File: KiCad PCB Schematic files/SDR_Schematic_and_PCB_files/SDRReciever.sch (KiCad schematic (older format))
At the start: 80 parts, among them J1 Conn_Coaxial, J10 I_0, J11 I_180, J12 Q_90, J13 Q_270, J14 I_OUT, J15 Q_OUT, J16 5V, J17 4.3V, J18 Conn_01x02_Female, J19 Conn_01x02_Female, J2 AudioJack3, J3 FIL_I, J4 FIL_O, J5 CLK_1, J6 CLK_2, J7 CLK_0, J8 I_LO, J9 Q_LO, Q1 PN2222A, U1 Si5351A-B-GT, U2 74AC74, U3 SN74CBT3253, U4 INA821ID, U5 INA821ID, U6 OP213FPZ, U7 LM741, Y1 ATS250

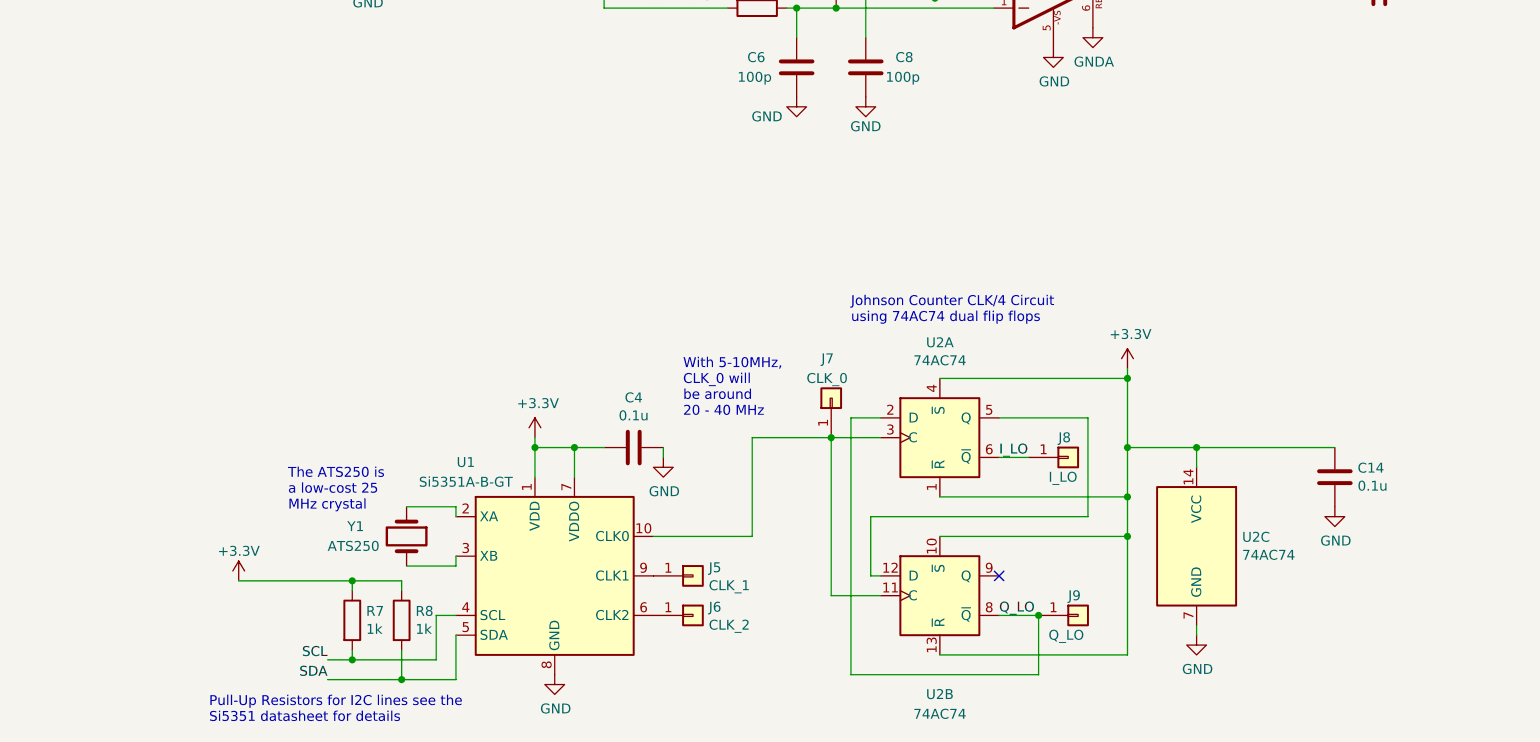
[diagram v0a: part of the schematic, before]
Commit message: Removed unnecessary files and components
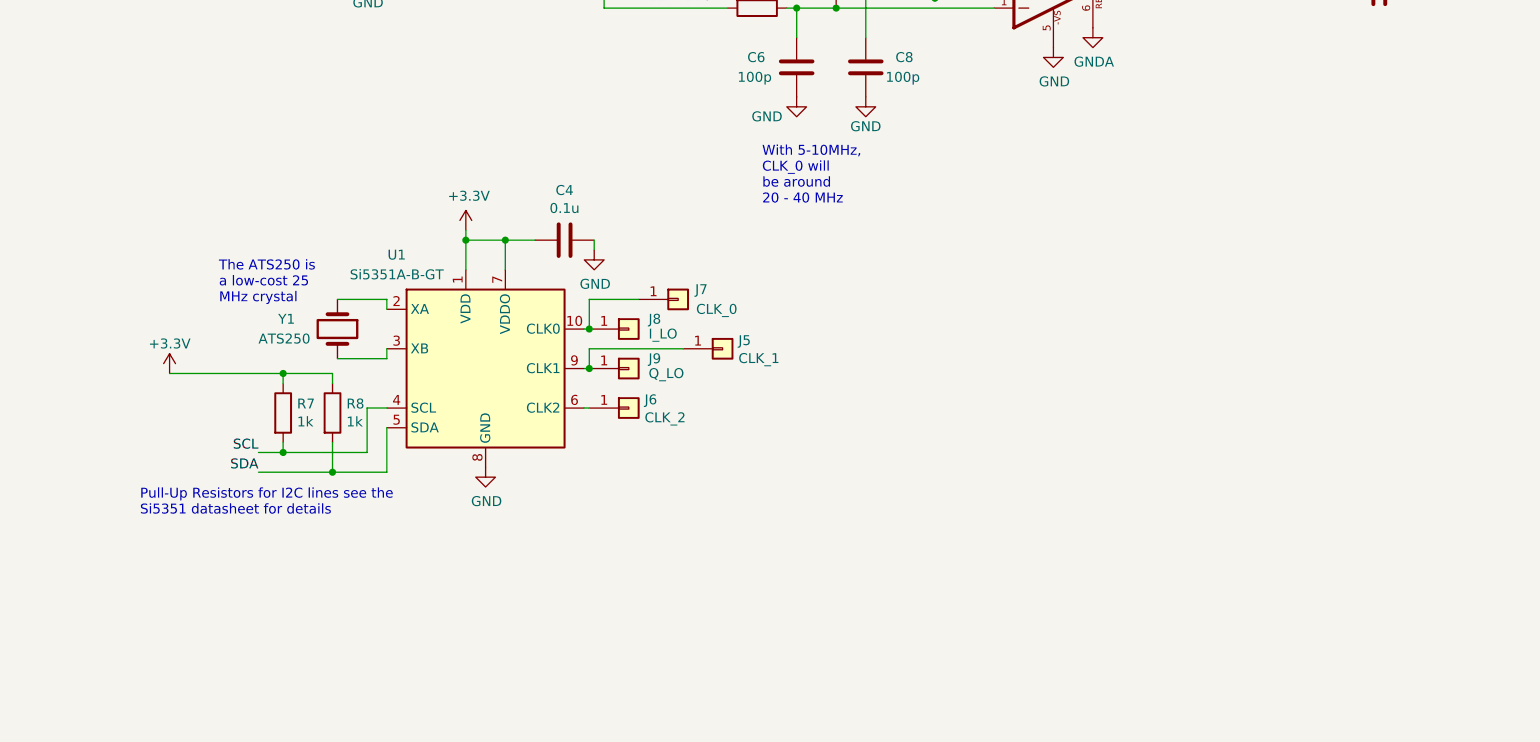
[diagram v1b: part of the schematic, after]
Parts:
- removed C14: 0.1u, Capacitor_THT:C_Disc_D5.1mm_W3.2mm_P5.00mm, symbol SDRReciever-rescue:C-Device
- removed U2: 74AC74, Package_DIP:DIP-14_W7.62mm, symbol SDRReciever-rescue:74HC74-74xx
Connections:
- net I_LO: no longer J8.1 (Pin_1)
- net Q_LO: no longer J9.1 (Pin_1)
- net at J7.1 (Pin_1), U1.10 (CLK0): now also J8.1 (Pin_1)
- net at J5.1 (Pin_1), U1.9 (CLK1): now also J9.1 (Pin_1)
- no-connect marks 27 -> 26
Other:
- note removed: "Johnson Counter CLK/4 Circuit\nusing 74AC74 dual flip flops"
- moved on the sheet: C4, J5, J6, J7, J8, J9, R7, R8, U1, Y1

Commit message: Updated values for bandpass filter in KiCad schematic Now a 3-rd order, series first, butterworth filter passing 6-16Mhz Also added some additional comments to KiCad schematic
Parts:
- removed RV1: 100k, symbol SDRReciever-rescue:R_POT-Device
- added R18, R19: 10k, Resistor_THT:R_Axial_DIN0207_L6.3mm_D2.5mm_P7.62mm_Horizontal, symbol SDRReciever-rescue:R-Device
- C2: value 910pF -> 330pF
- C3: value 150pF -> 330pF
- L1: value 820nH -> 430nH
- L2: value 560nH -> 820nH
- L3: value 3.6uH -> 820nH
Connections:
- net +4.3V: now also R18.2
- net BPF_OUT: now also R18.1, R19.2
- net GND: now also R19.1
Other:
- note added: "2.15V Voltage Bias to center\nthe incoming frequency between \nmax and min input values for tayloe mixer"
- note added: "6-16MHz (3rd Order, Series-First Butterworth)\nBy doing Series-First, DC signals cannot pass through the capacitor (C2), \nallowing better control over the DC offset going into the op-amps"
- note added: "Amplifiers"
- note added: "Antenna Connector"
- note added: "Arduino Nano"
- note added: "Bandpass Filter"
- note added: "C5-C8 are sampling\ncapacitors which also\nact as low pass filters here"
- note added: "Final Output\n(to soundcard)"
- note added: "Local Oscillator (Si5351a)"
- note added: "Low Pass Filter (2-Pole)"
- note added: "NOTE:\nDouble check values of C5-C8"
- note added: "T37-6 Toroid:\n-- turns"
- note added: "T50-6 Toroid: \n-- turns"
- note added: "Tayloe Mixer"
- note added: "Test point pad"
- note added: "To smooth 5V power supply from\nUSB which may contain noise"
- note added: "Voltage Smoother"
- note removed: "Bandpass Filter 5-18MHz (3rd Order, Series-First Bessel)\nBy doing Series-First, DC signals cannot pass through the capacitor (C2), \nallowing better control over the DC offset going into the op-amps"
- note removed: "T37-6 Toroid:\n17 turns"
- note removed: "T50-6 Toroid: \n12 turns"
- note removed: "T50-6 Toroid: \n30 turns"
- note removed: "Tunable\n2.15V Bias"
- note removed: "With 5-10MHz, \nCLK_0 will \nbe around \n20 - 40 MHz"
- moved on the sheet: A1, C11, C12, C13, C4, J5, J6, J7, J8, J9, JP2, R7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

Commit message: Updated schematic, added voltage converter and comments
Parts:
- removed J8: I_LO, Connector_PinHeader_2.54mm:PinHeader_1x01_P2.54mm_Vertical, symbol SDRReciever-rescue:Conn_01x01-Connector_Generic
- removed J9: Q_LO, Connector_PinHeader_2.54mm:PinHeader_1x01_P2.54mm_Vertical, symbol SDRReciever-rescue:Conn_01x01-Connector_Generic
- added Q2, Q3: BSS138, Package_TO_SOT_SMD:SOT-23, symbol Device:Q_NMOS_GSD
- added R20, R21, R22, R23: 10k, Resistor_SMD:R_0805_2012Metric, symbol SDRReciever-rescue:R-Device
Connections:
- net +3V3: now also Q2.1 (G), Q3.1 (G), R20.1, R21.1
- net +4.3V: now also U7.7 (V+)
- net +5V: now also R22.1, R23.1; no longer U7.7 (V+)
- net I_LO: now also J7.1 (Pin_1), U1.10 (CLK0)
- net Q_LO: now also J5.1 (Pin_1), U1.9 (CLK1)
- net SCL renamed SCL_3V
- net SCL_3V: now also Q3.2 (S), R21.2; no longer A1.24 (A5)
- net SDA renamed SDA_3V
- net SDA_3V: now also Q2.2 (S), R20.2; no longer A1.23 (A4)
- new net SCL_5V: A1.24 (A5), Q3.3 (D), R23.2
- new net SDA_5V: A1.23 (A4), Q2.3 (D), R22.2
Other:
- note added: "5V to 3.3V Conveter"
- note added: "NOTE: maybe split the gain between these two op amp stages (especially if the later stage is low noise)"
- note added: "NOTE: use Lower noise op amp"
- note added: "NOTE:\nDouble check values of C5-C8\n100nf?"
- note added: "Note:\nCheck all footprints\nExchange some through hole components for surface mount"
- note added: "This is used to convert the\n5V logic of the arduino nano\nto the 3.3V logic of the Si5351a\nboth directions."
- note removed: "NOTE:\nDouble check values of C5-C8"
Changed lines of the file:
@@
 EESchema Schematic File Version 4
-LIBS:SDRReciever-cache
-EELAYER 26 0
+EELAYER 30 0
 EELAYER END
 $Descr A1 33110 23386
@@
 $EndComp
 Text Label 14250 4725 1    50   ~ 0
-SDA
+SDA_5V
 Text Label 14350 4725 1    50   ~ 0
-SCL
+SCL_5V
 $Comp
 L SDRReciever-rescue:+3.3V-power #PWR02
@@
 $EndComp
 Text Label 7475 5850 2    50   ~ 0
-SDA
+SDA_3V
 Text Label 7475 5750 2    50   ~ 0
-SCL
+SCL_3V
 $Comp
 L SDRReciever-rescue:Jumper_NC_Small-Device JP2
@@
 $EndComp
 $Comp
-L SDRReciever-rescue:Conn_01x01-Connector_Generic J8
-U 1 1 5EAFA8DE
-P 9350 5125
-F 0 "J8" H 9450 5175 50  0000 L CNN
-F 1 "I_LO" H 9450 5100 50  0000 L CNN
-F 2 "Connector_PinHeader_2.54mm:PinHeader_1x01_P2.54mm_Vertical" H 9350 5125 50  0001 C CNN
-F 3 "~" H 9350 5125 50  0001 C CNN
-	1    9350 5125
-	1    0    0    -1
-$EndComp
-$Comp
-L SDRReciever-rescue:Conn_01x01-Connector_Generic J9
-U 1 1 5EB14DFD
-P 9350 5325
-F 0 "J9" H 9450 5375 50  0000 L CNN
-F 1 "Q_LO" H 9450 5300 50  0000 L CNN
-F 2 "Connector_PinHeader_2.54mm:PinHeader_1x01_P2.54mm_Vertical" H 9350 5325 50  0001 C CNN
-F 3 "~" H 9350 5325 50  0001 C CNN
-	1    9350 5325
-	1    0    0    -1
-$EndComp
-$Comp
 L SDRReciever-rescue:C-Device C17
 U 1 1 5EA7D591
@@
 	1    0    0    -1
 $EndComp
-$Comp
-L SDRReciever-rescue:+5V-power #PWR042
-U 1 1 5EDC9E45
-P 4625 4325
-F 0 "#PWR042" H 4625 4175 50  0001 C CNN
-F 1 "+5V" H 4775 4375 50  0000 C CNN
-F 2 "" H 4625 4325 50  0001 C CNN
-F 3 "" H 4625 4325 50  0001 C CNN
-	1    4625 4325
-	1    0    0    -1
-$EndComp
 Wire Wire Line
 	4425 4725 4325 4725
@@
 	5025 4625 5425 4625
 Connection ~ 5025 4625
-Text Notes 4125 4150 0    50   ~ 0
+Text Notes 4175 4075 0    50   ~ 0
 The INA821ID Amps require the REF\ninput to have a voltage source with a\nlow output impedence. The LM741\nvoltage buffer handles this
 Wire Wire Line
@@
 Wire Notes Line
 	5000 1600 5000 1650
-Text Notes 6875 6075 0    50   ~ 0
+Text Notes 6875 6175 0    50   ~ 0
 Pull-Up Resistors for I2C lines see the \nSi5351 datasheet for details
 Wire Wire Line
@@
 Wire Wire Line
 	9150 5325 9125 5325
-Connection ~ 9150 5325
 Wire Wire Line
 	9150 5125 9125 5125
-Connection ~ 9150 5125
 Wire Wire Line
 	9150 5525 9125 5525
@@
 Amplifiers
 Text Notes 6400 2775 0    50   ~ 0
-NOTE:\nDouble check values of C5-C8
+NOTE:\nDouble check values of C5-C8\n100nf?
+Text Notes 4600 5600 0    50   ~ 0
+NOTE: use Lower noise op amp
+Text Notes 13250 3800 0    50   ~ 0
+NOTE: maybe split the gain between these two op amp stages (especially if the later stage is low noise)
+$Comp
+L SDRReciever-rescue:R-Device R20
+U 1 1 607EFC63
+P 2400 7025
+F 0 "R20" H 2470 7071 50  0000 L CNN
+F 1 "10k" H 2470 6980 50  0000 L CNN
+F 2 "Resistor_SMD:R_0805_2012Metric" V 2330 7025 50  0001 C CNN
+F 3 "~" H 2400 7025 50  0001 C CNN
+	1    2400 7025
+	1    0    0    -1
+$EndComp
+Wire Wire Line
+	4050 6825 4050 6875
+Wire Wire Line
+	4450 6825 4450 6875
+Wire Wire Line
+	2400 6825 2800 6825
+Connection ~ 2400 6825
+Wire Wire Line
+	2400 6825 2400 6875
+Connection ~ 2800 6825
+Wire Wire Line
+	4050 6825 4450 6825
+Connection ~ 4450 6825
+$Comp
+L Device:Q_NMOS_GSD Q3
+U 1 1 608C951F
+P 3750 8025
+F 0 "Q3" V 3999 8025 50  0000 C CNN
+F 1 "BSS138" V 4090 8025 50  0000 C CNN
+F 2 "Package_TO_SOT_SMD:SOT-23" H 3950 8125 50  0001 C CNN
+F 3 "~" H 3750 8025 50  0001 C CNN
+	1    3750 8025
+	0    1    1    0
+$EndComp
+Wire Wire Line
+	3550 8125 2800 8125
+$Comp
+L Device:Q_NMOS_GSD Q2
+U 1 1 608B7971
+P 3200 7325
+F 0 "Q2" V 3449 7325 50  0000 C CNN
+F 1 "BSS138" V 3540 7325 50  0000 C CNN
+F 2 "Package_TO_SOT_SMD:SOT-23" H 3400 7425 50  0001 C CNN
+F 3 "~" H 3200 7325 50  0001 C CNN
+	1    3200 7325
+	0    1    1    0
+$EndComp
+Wire Wire Line
+	3200 6825 3200 7125
+Wire Wire Line
+	3200 6825 3750 6825
+Wire Wire Line
+	3750 6825 3750 7825
+Connection ~ 3200 6825
+Wire Wire Line
+	4050 7175 4050 7425
+Wire Wire Line
+	4050 7425 3400 7425
+Wire Wire Line
+	4450 8125 3950 8125
+Wire Wire Line
+	4450 7175 4450 7775
+Wire Wire Line
+	2400 7175 2400 7425
+Connection ~ 2400 7425
+Wire Wire Line
+	2800 6825 2800 6875
+Wire Wire Line
+	2800 6825 3200 6825
+Wire Wire Line
+	2800 7175 2800 8125
+Connection ~ 2800 8125
+Wire Wire Line
+	2800 8125 2100 8125
+Wire Wire Line
+	4450 6675 4450 6825
+Wire Wire Line
+	4450 7775 4750 7775
+Connection ~ 4450 7775
+Wire Wire Line
+	4450 7775 4450 8125
+Text Label 4750 7775 0    50   ~ 0
+SCL_5V
+Text Label 4150 7425 0    50   ~ 0
+SDA_5V
+Text Label 2100 7425 2    50   ~ 0
+SDA_3V
+Text Label 2100 8125 2    50   ~ 0
+SCL_3V
+Wire Wire Line
+	2400 7425 2100 7425
+Wire Wire Line
+	2400 7425 3000 7425
+$Comp
+L SDRReciever-rescue:+5V-power #PWR030
+U 1 1 60A07087
+P 4450 6675
+F 0 "#PWR030" H 4450 6525 50  0001 C CNN
+F 1 "+5V" H 4465 6848 50  0000 C CNN
+F 2 "" H 4450 6675 50  0001 C CNN
+F 3 "" H 4450 6675 50  0001 C CNN
+	1    4450 6675
+	1    0    0    -1
+$EndComp
+$Comp
+L SDRReciever-rescue:+3.3V-power #PWR05
+U 1 1 60A07AAF
+P 2400 6650
+F 0 "#PWR05" H 2400 6500 50  0001 C CNN
+F 1 "+3.3V" H 2415 6823 50  0000 C CNN
+F 2 "" H 2400 6650 50  0001 C CNN
+F 3 "" H 2400 6650 50  0001 C CNN
+	1    2400 6650
+	1    0    0    -1
+$EndComp
+$Comp
+L 4V3Power:+4.3V #PWR04
+U 1 1 60A1FEE2
+P 4625 4325
+F 0 "#PWR04" H 4625 4175 50  0001 C CNN
+F 1 "+4.3V" H 4640 4498 50  0000 C CNN
+F 2 "" H 4625 4325 50  0001 C CNN
+F 3 "" H 4625 4325 50  0001 C CNN
+	1    4625 4325
+	1    0    0    -1
+$EndComp
+$Comp
+L SDRReciever-rescue:R-Device R21
+U 1 1 60A20952
+P 2800 7025
+F 0 "R21" H 2870 7071 50  0000 L CNN
+F 1 "10k" H 2870 6980 50  0000 L CNN
+F 2 "Resistor_SMD:R_0805_2012Metric" V 2730 7025 50  0001 C CNN
+F 3 "~" H 2800 7025 50  0001 C CNN
+	1    2800 7025
+	1    0    0    -1
+$EndComp
+$Comp
+L SDRReciever-rescue:R-Device R22
+U 1 1 60A20C11
+P 4050 7025
+F 0 "R22" H 4120 7071 50  0000 L CNN
+F 1 "10k" H 4120 6980 50  0000 L CNN
+F 2 "Resistor_SMD:R_0805_2012Metric" V 3980 7025 50  0001 C CNN
+F 3 "~" H 4050 7025 50  0001 C CNN
+	1    4050 7025
+	1    0    0    -1
+$EndComp
+$Comp
+L SDRReciever-rescue:R-Device R23
+U 1 1 60A20F9E
+P 4450 7025
+F 0 "R23" H 4520 7071 50  0000 L CNN
+F 1 "10k" H 4520 6980 50  0000 L CNN
+F 2 "Resistor_SMD:R_0805_2012Metric" V 4380 7025 50  0001 C CNN
+F 3 "~" H 4450 7025 50  0001 C CNN
+	1    4450 7025
+	1    0    0    -1
+$EndComp
+Text Notes 3700 6050 2    50   ~ 10
+5V to 3.3V Conveter
+Text Notes 3900 6400 2    50   ~ 0
+This is used to convert the\n5V logic of the arduino nano\nto the 3.3V logic of the Si5351a\nboth directions.
+Text Label 9150 5125 0    50   ~ 0
+I_LO
+Text Label 9150 5325 0    50   ~ 0
+Q_LO
+Wire Wire Line
+	2400 6650 2400 6825
+Wire Wire Line
+	4050 7425 4150 7425
+Connection ~ 4050 7425
+Text Notes 10075 7275 0    50   ~ 0
+Note:\nCheck all footprints\nExchange some through hole components for surface mount
 $EndSCHEMATC
